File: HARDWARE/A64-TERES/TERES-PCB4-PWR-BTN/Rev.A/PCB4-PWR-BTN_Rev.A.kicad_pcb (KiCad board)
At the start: 2 copper layers, 36 x 10 mm, 8 parts, among them P1 CONN_01X06, SW1 SW_PUSH

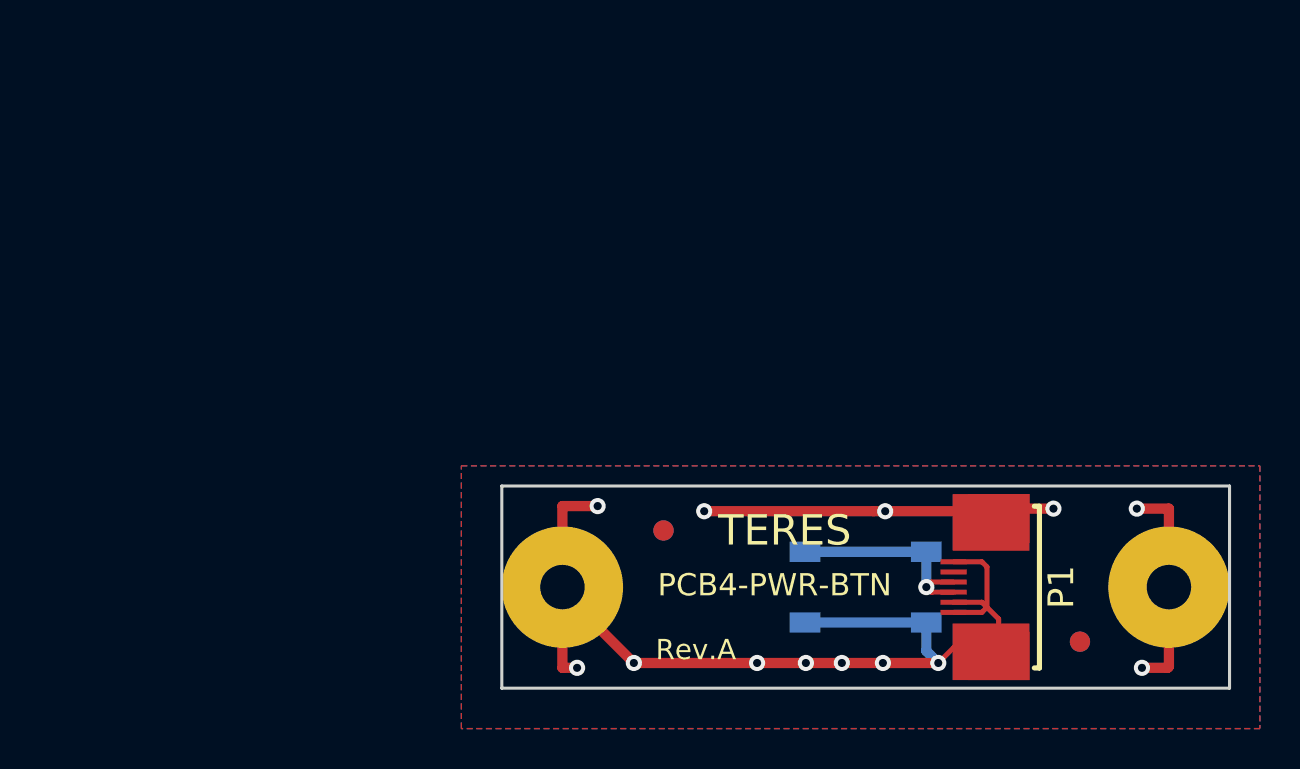
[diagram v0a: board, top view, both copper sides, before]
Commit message: PCB4_PWR_BTN_A: Update KiCAD and docs
* Updated on KiCAD 6.0.3
* Added Stack-up table and graphics
* Added General Notes to the gerber
* Replaced BOM with generated one
* Added README using export from gerber
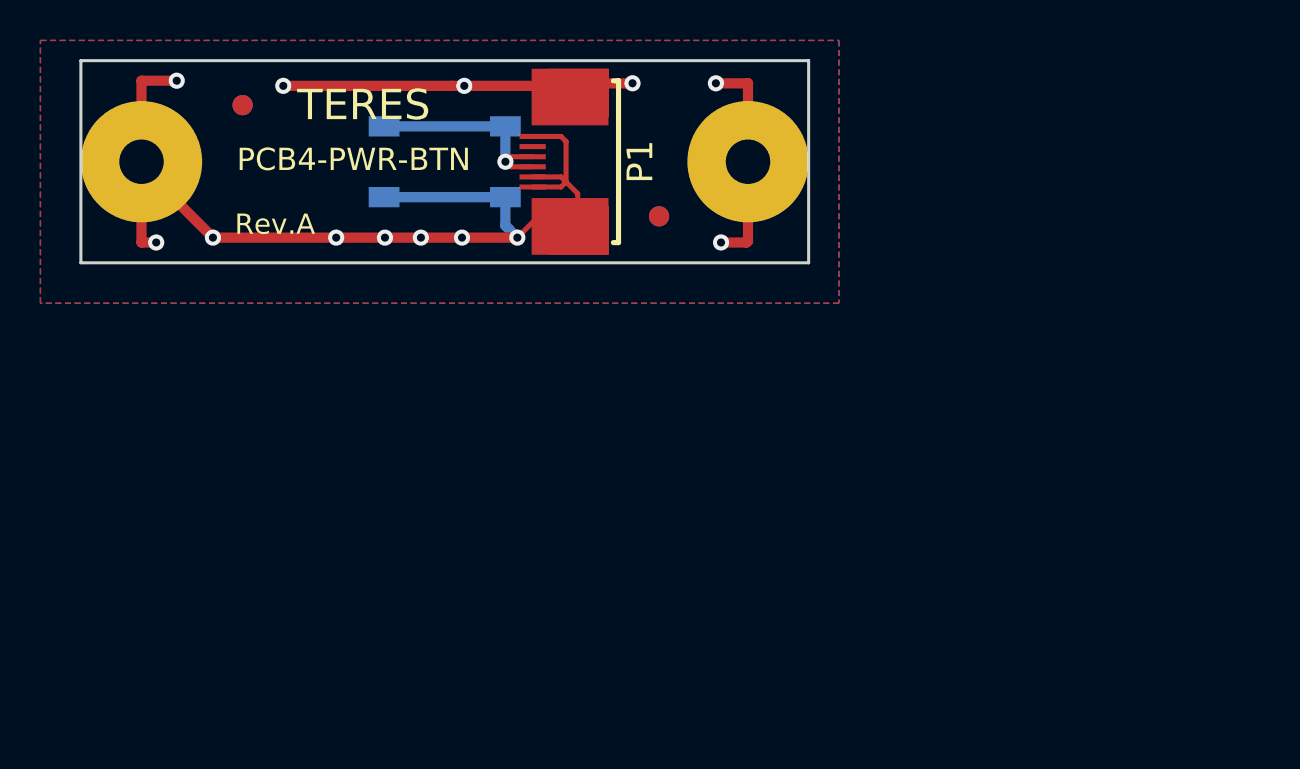
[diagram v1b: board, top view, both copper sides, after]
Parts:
- P1: value CONN_01X06 -> WZA21-06
- moved ? 29.6 mm to (97.8, 56.7) (x2)
- moved ? 29.6 mm to (77.2, 51.2) (x2)
- moved MountingHole 29.6 mm to (72.2, 54.0)
- moved MountingHole 29.6 mm to (102.2, 54.0)
- moved P1 29.6 mm to (93.7, 54.0)
- moved SW1 29.6 mm to (87.2, 54.0)
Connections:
- P1 pad 0: GND -> (no net)
- P1 pad 5: (no net) -> unconnected-(P1-Pad5)
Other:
- net class Default removed
- board text added: "0"
- board text added: "0 mm"
- board text added: "0,01 mm"
- board text added: "0,02"
- board text added: "0,035 mm"
- board text added: "1"
- board text added: "1,51 mm"
- board text added: "1. FABRICATE PER ANSI/IPC-A-600.IPC-QE-605.IPC-4552 AND IPC-SM-840 SPECIFICATIONS. 2. USE ROHS-COMPLIANT MATERIALS. 3. SOLDERMASK BOTH SIDES OF THE BOARD OVER BARE COPPER WITH MATERIALS PER ANSI/IPC-SM-840. 4. SEE FABRICATION FILES WITH SAME TITLE OR DRAWING, AND REVISION, AS THIS DRAWING 5. APPLY SILKSCREEN TO BOTH SIDES OF THE BOARD USING NON-CONDUCTIVE EPOXY INK 6. SEE SEPARATE DRILL FILE FOR 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"
- board text added: "3,3"
- board text added: "4,5"
- board text added: "B.Cu"
- board text added: "B.Mask"
- board text added: "B.Paste"
- board text added: "B.Silkscreen"
- board text added: "BOTTOM LAYER"
- board text added: "Bottom Silk Screen"
- board text added: "Bottom Solder Mask"
- board text added: "Bottom Solder Paste"
- board text added: "Dielectric 1"
- board text added: "Epsilon R"
- board text added: "F.Cu"
- board text added: "F.Mask"
- board text added: "F.Paste"
- board text added: "F.Silkscreen"
- board text added: "FR4"
- board text added: "FRONT LAYER"
- board text added: "GENERAL NOTES"
- board text added: "LAYER DETAIL"
- board text added: "Layer Name"
- board text added: "Loss Tangent"
- board text added: "Material"
- board text added: "Not specified"
- board text added: "Recommended Color"
- board text added: "Red"
- board text added: "SOLDER MASK BOTTOM (B.Cu)"
- board text added: "SOLDER MASK FRONT (F.Cu)"
- board text added: "Spacer e.g. FR4"
- board text added: "Thickness (mm)"
- board text added: "Top Silk Screen"
- board text added: "Top Solder Mask"
- board text added: "Top Solder Paste"
- board text added: "Type"
- board text added: "White"
- board text added: "copper"
- board text added: "core"
